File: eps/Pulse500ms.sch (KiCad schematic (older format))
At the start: 5 parts, among them U3 TLC555xPS

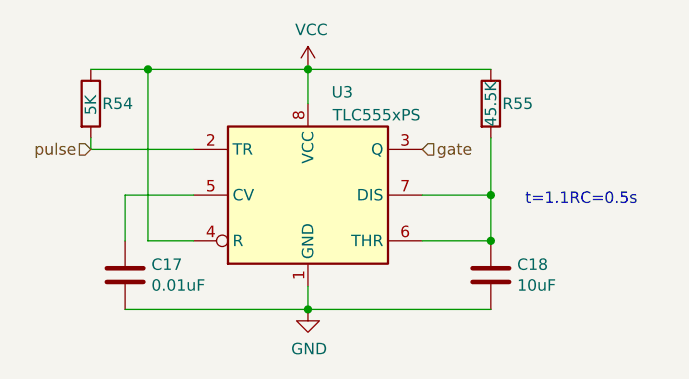
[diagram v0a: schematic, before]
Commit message: switch vcc to 3.3v, add battery switching mosfet
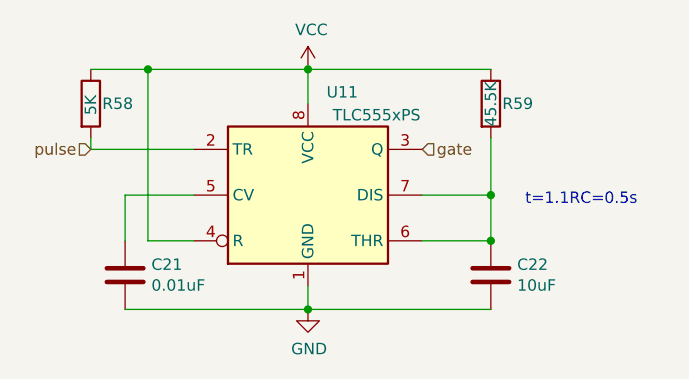
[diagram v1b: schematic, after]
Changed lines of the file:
@@
 $Descr A4 11693 8268
 encoding utf-8
-Sheet 3 7
+Sheet 4 7
 Title ""
 Date ""
@@
 AR Path="/619279C9/619CA4E2/619C833F" Ref="U10"  Part="1"
 AR Path="/619279C9/619D4C5F/619C833F" Ref="U11"  Part="1"
-F 0 "U3" H 5500 3850 50  0000 C CNN
+F 0 "U11" H 5500 3850 50  0000 C CNN
 F 1 "TLC555xPS" H 5650 3750 50  0000 C CNN
 F 2 "Package_SO:VSSOP-8_3.0x3.0mm_P0.65mm" H 6000 3000 50  0001 C CNN
@@
 AR Path="/619279C9/619CA4E2/619C8346" Ref="#PWR047"  Part="1"
 AR Path="/619279C9/619D4C5F/619C8346" Ref="#PWR049"  Part="1"
-F 0 "#PWR045" H 5350 2700 50  0001 C CNN
+F 0 "#PWR049" H 5350 2700 50  0001 C CNN
 F 1 "VCC" H 5365 3023 50  0000 C CNN
 F 2 "" H 5350 2850 50  0001 C CNN
@@
 AR Path="/619279C9/619CA4E2/619C834D" Ref="R56"  Part="1"
 AR Path="/619279C9/619D4C5F/619C834D" Ref="R58"  Part="1"
-F 0 "R54" H 4450 3000 50  0000 L CNN
+F 0 "R58" H 4450 3000 50  0000 L CNN
 F 1 "5K" V 4400 2950 50  0000 L CNN
 F 2 "" V 4330 3000 50  0001 C CNN
@@
 AR Path="/619279C9/619CA4E2/619C835C" Ref="R57"  Part="1"
 AR Path="/619279C9/619D4C5F/619C835C" Ref="R59"  Part="1"
-F 0 "R55" H 6200 3000 50  0000 L CNN
+F 0 "R59" H 6200 3000 50  0000 L CNN
 F 1 "45.5K" V 6150 2900 50  0000 L CNN
 F 2 "" V 6080 3000 50  0001 C CNN
@@
 AR Path="/619279C9/619CA4E2/619C8368" Ref="C20"  Part="1"
 AR Path="/619279C9/619D4C5F/619C8368" Ref="C22"  Part="1"
-F 0 "C18" H 6265 3796 50  0000 L CNN
+F 0 "C22" H 6265 3796 50  0000 L CNN
 F 1 "10uF" H 6265 3705 50  0000 L CNN
 F 2 "" H 6188 3600 50  0001 C CNN
@@
 AR Path="/619279C9/619CA4E2/619C836F" Ref="C19"  Part="1"
 AR Path="/619279C9/619D4C5F/619C836F" Ref="C21"  Part="1"
-F 0 "C17" H 4665 3796 50  0000 L CNN
+F 0 "C21" H 4665 3796 50  0000 L CNN
 F 1 "0.01uF" H 4665 3705 50  0000 L CNN
 F 2 "" H 4588 3600 50  0001 C CNN
@@
 AR Path="/619279C9/619CA4E2/619C837B" Ref="#PWR048"  Part="1"
 AR Path="/619279C9/619D4C5F/619C837B" Ref="#PWR050"  Part="1"
-F 0 "#PWR046" H 5350 3650 50  0001 C CNN
+F 0 "#PWR050" H 5350 3650 50  0001 C CNN
 F 1 "GND" H 5355 3727 50  0000 C CNN
 F 2 "" H 5350 3900 50  0001 C CNN

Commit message: update pcbnew
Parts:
- C17, C18: footprint (none) -> Capacitor_SMD:C_0805_2012Metric_Pad1.18x1.45mm_HandSolder
- R54, R55: footprint (none) -> Resistor_SMD:R_0805_2012Metric_Pad1.20x1.40mm_HandSolder
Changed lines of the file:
@@
 F 0 "R58" H 4450 3000 50  0000 L CNN
 F 1 "5K" V 4400 2950 50  0000 L CNN
-F 2 "" V 4330 3000 50  0001 C CNN
+F 2 "Resistor_SMD:R_0805_2012Metric_Pad1.20x1.40mm_HandSolder" V 4330 3000 50  0001 C CNN
 F 3 "~" H 4400 3000 50  0001 C CNN
 	1    4400 3000
@@
 F 0 "R59" H 6200 3000 50  0000 L CNN
 F 1 "45.5K" V 6150 2900 50  0000 L CNN
-F 2 "" V 6080 3000 50  0001 C CNN
+F 2 "Resistor_SMD:R_0805_2012Metric_Pad1.20x1.40mm_HandSolder" V 6080 3000 50  0001 C CNN
 F 3 "~" H 6150 3000 50  0001 C CNN
 	1    6150 3000
@@
 F 0 "C22" H 6265 3796 50  0000 L CNN
 F 1 "10uF" H 6265 3705 50  0000 L CNN
-F 2 "" H 6188 3600 50  0001 C CNN
+F 2 "Capacitor_SMD:C_0805_2012Metric_Pad1.18x1.45mm_HandSolder" H 6188 3600 50  0001 C CNN
 F 3 "~" H 6150 3750 50  0001 C CNN
 	1    6150 3750
@@
 F 0 "C21" H 4665 3796 50  0000 L CNN
 F 1 "0.01uF" H 4665 3705 50  0000 L CNN
-F 2 "" H 4588 3600 50  0001 C CNN
+F 2 "Capacitor_SMD:C_0805_2012Metric_Pad1.18x1.45mm_HandSolder" H 4588 3600 50  0001 C CNN
 F 3 "~" H 4550 3750 50  0001 C CNN
 	1    4550 3750
